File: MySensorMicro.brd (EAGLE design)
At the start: 17.7 x 30.5 mm, 23 parts, among them IC1 MEGA328P-AU, IC2 AT25DF512C-SSHN-B, IC3 SI7021, IC4 ATSHA204A, Q1 N/M

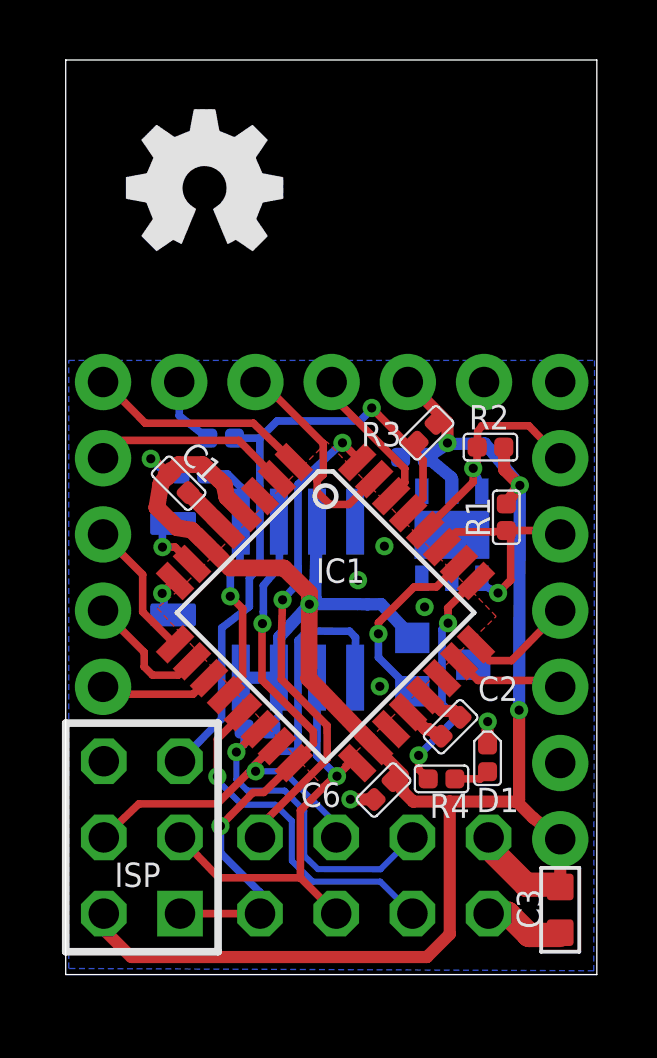
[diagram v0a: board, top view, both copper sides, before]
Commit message: Adapt PCB layout to 0603 package size "major change"
* Schematic
- rotate C5
- delete X1 "crystal"

* PCB Layout "major change"

- Change board size to 19.5x17.5
- All passive componets are changed to 0603 package size
- Delete SI7021 sensor
- Delete C4 and renumbering capacitors' numbers
- Delete R4 and renumbering resisots' numbers
- Delete D1
- Delete Q1 crystal

* Full re-arrangment of passive componets to fit the new 0603

- Moved C4, R3 to button layer
- All other passive componets have been reoriented
- Moved the eeprom chip a few milli meters above so that R4 can fit

** This version has been checked for DRC
** This version will be reviewed again ana make sure all pins are
connected correctly and nothing is missing
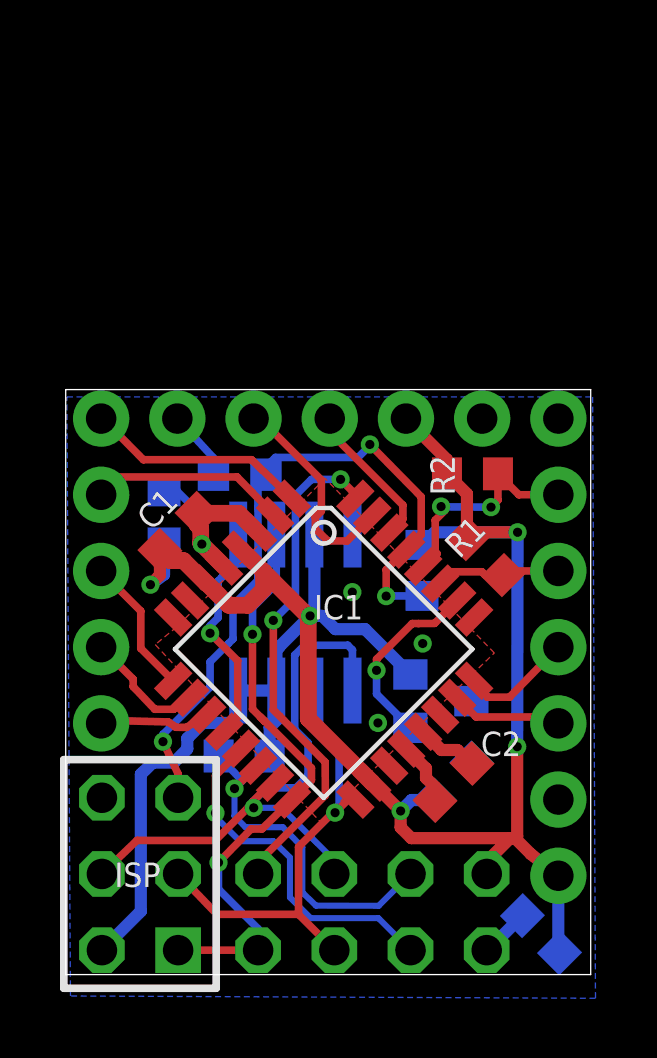
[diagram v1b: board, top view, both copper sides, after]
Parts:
- removed C6: 100n, Discrete:C0402
- removed D1: (no value), Discrete:LED-0402
- removed IC3: SI7021, Sensor:DFN6
- removed Q1: N/M, Discrete:2P-L3.2XW1.5MM
- removed R6: 56k, Discrete:R0402
- C1, C2, C4, C5: device Discrete:C0402 -> resistor:C0603K
- C3: device Discrete:C0603 -> resistor:C0603K
- R1, R2, R3, R5: device Discrete:R0402 -> resistor:R0603
- R4: value 330 -> 56k; device Discrete:R0402 -> resistor:R0603
- moved C4 10.9 mm to (12.9, 6.44), turned to 135 degrees
- moved R4 6.62 mm to (5.95, 7.28), flipped to the bottom, turned to 180 degrees
- moved R3 4.59 mm to (11.9, 13.5), flipped to the bottom, turned to 90 degrees
- moved C2 1.84 mm to (12.9, 6.42)
- moved R5 1.73 mm to (3.28, 15.3), turned to 270 degrees
- moved C1 1.62 mm to (3.76, 14.8), turned to 45 degrees
- moved R1 1.51 mm to (14.0, 13.9), turned to 135 degrees
- moved C5 1.37 mm to (5.80, 16.7)
- moved IC4 1.22 mm to (12.5, 9.12)
- moved JP2 1.22 mm to (16.4, 18.5)
- moved JP4 1.22 mm to (1.18, 18.5)
- moved JP5 1.22 mm to (16.4, 16.0)
- moved JP1 1.22 mm to (10.2, 2.08)
- moved JP3 1.22 mm to (2.48, 3.35)
- moved IC1 1.22 mm to (8.60, 10.8)
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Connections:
- removed net N$1: IC1.7, Q1.1
- removed net N$2: IC1.8, Q1.2
- removed net N$3: D1.+, R4.2
- net A2: no longer R4.1
- net D10: now also R4.1; no longer R6.1
- net GND: no longer C6.2, D1.-, IC3.2
- net SCL: no longer IC3.6
- net SDA: no longer IC3.1
- net V+: now also R4.2; no longer C6.1, IC3.5, R6.2
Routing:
- net A2: track 7.94 -> 0.00 mm, vias 2 -> 0
- net V+: track 82.6 -> 76.1 mm
- net SDA: track 8.26 -> 4.69 mm, vias 1 -> 0
- net D8: track 8.81 -> 12.0 mm
- net RST: track 21.3 -> 24.1 mm, vias 1 -> 3
- net N$1: track 2.19 -> 0.00 mm, vias 1 -> 0
- net N$2: track 1.56 -> 0.00 mm, vias 1 -> 0
- net N$3: track 1.19 -> 0.00 mm
- net MISO: track 18.8 -> 19.9 mm
- net MOSI: track 20.2 -> 21.3 mm
- net SCK: track 14.6 -> 15.6 mm
- net D2: track 16.5 -> 17.2 mm
- net N$4: track 1.40 -> 2.13 mm
- net GND: track 7.55 -> 8.18 mm, vias 6 -> 4
- net D10: track 11.3 -> 12.0 mm
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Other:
- board size 17.7 x 30.5 mm -> 17.5 x 19.5 mm
- board text removed: "D3"
